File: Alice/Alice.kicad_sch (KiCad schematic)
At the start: 0 parts

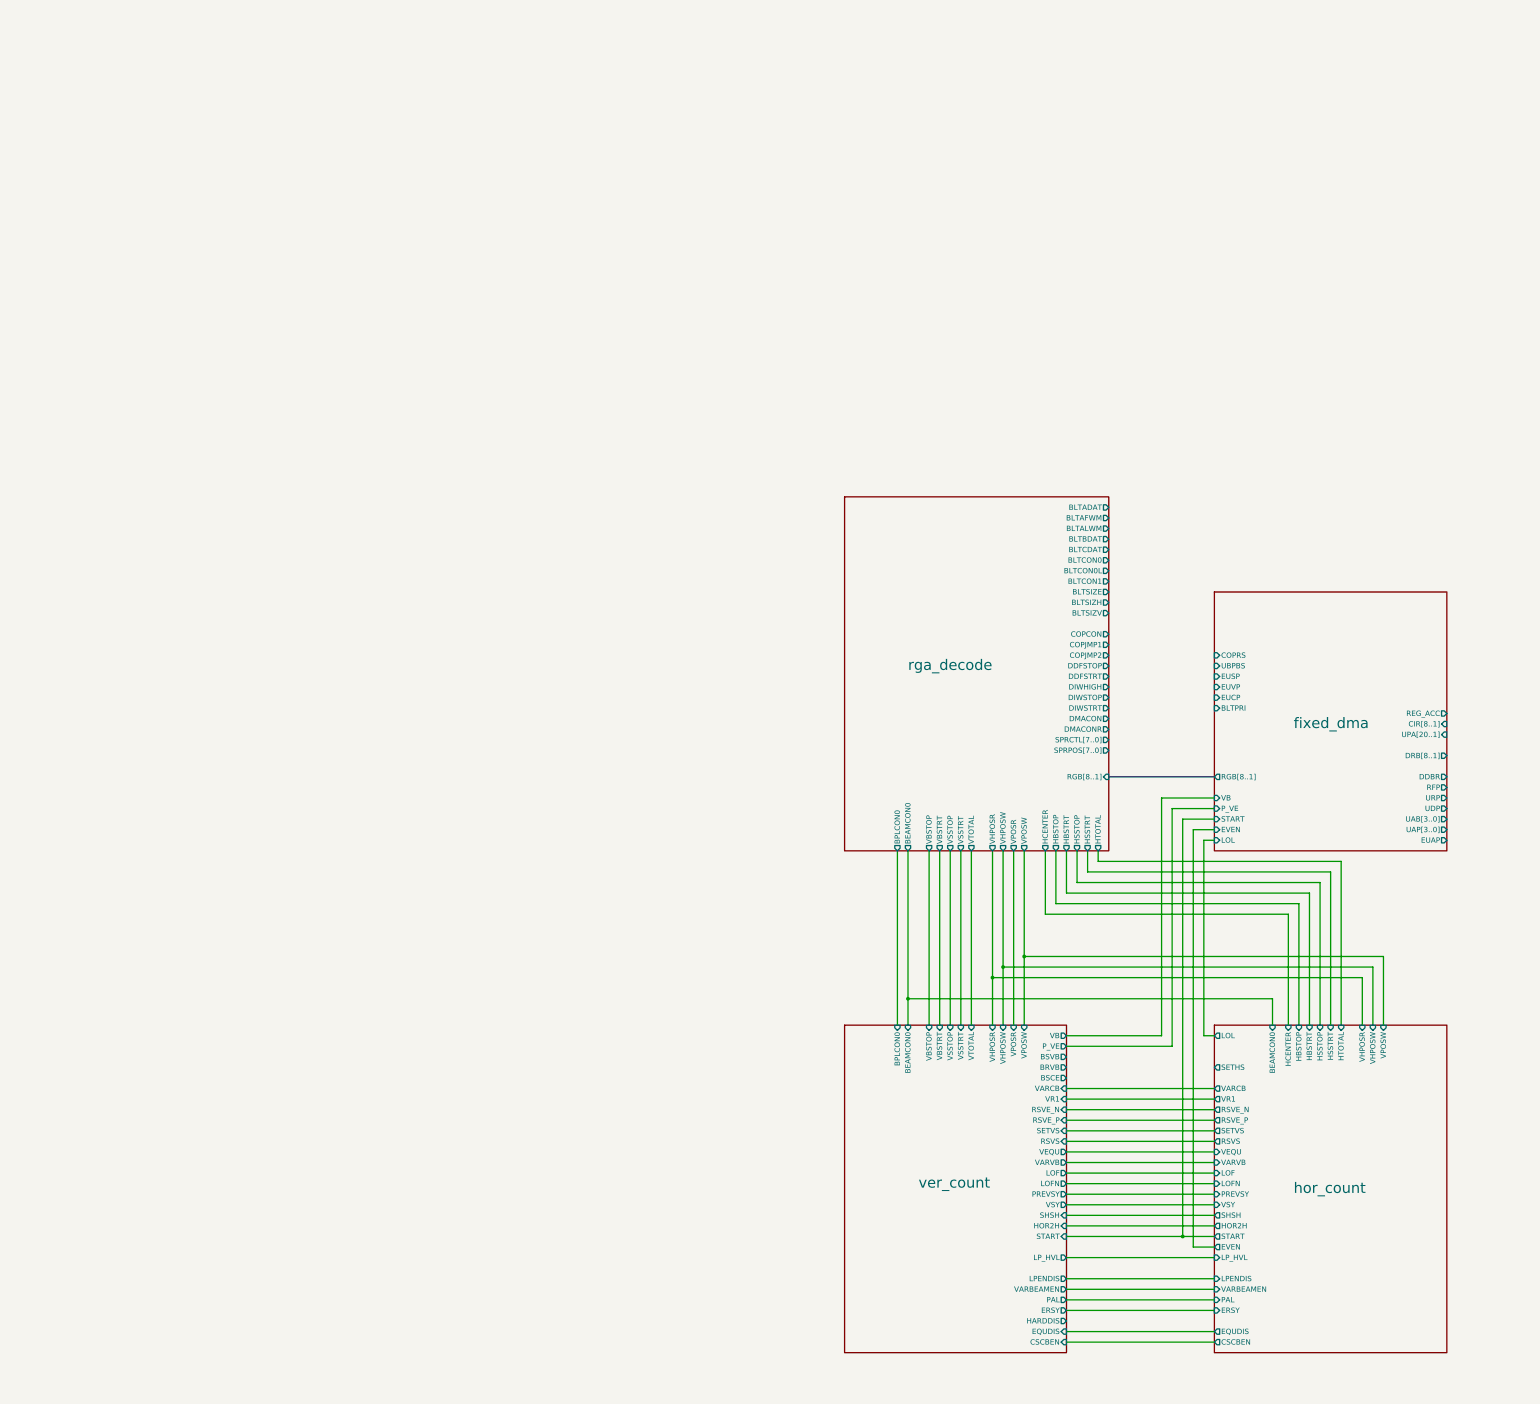
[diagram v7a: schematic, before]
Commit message: Some refactoring : BEAMCON0 and BPLCON0 moved to the top sheet, CLOCKGEN added
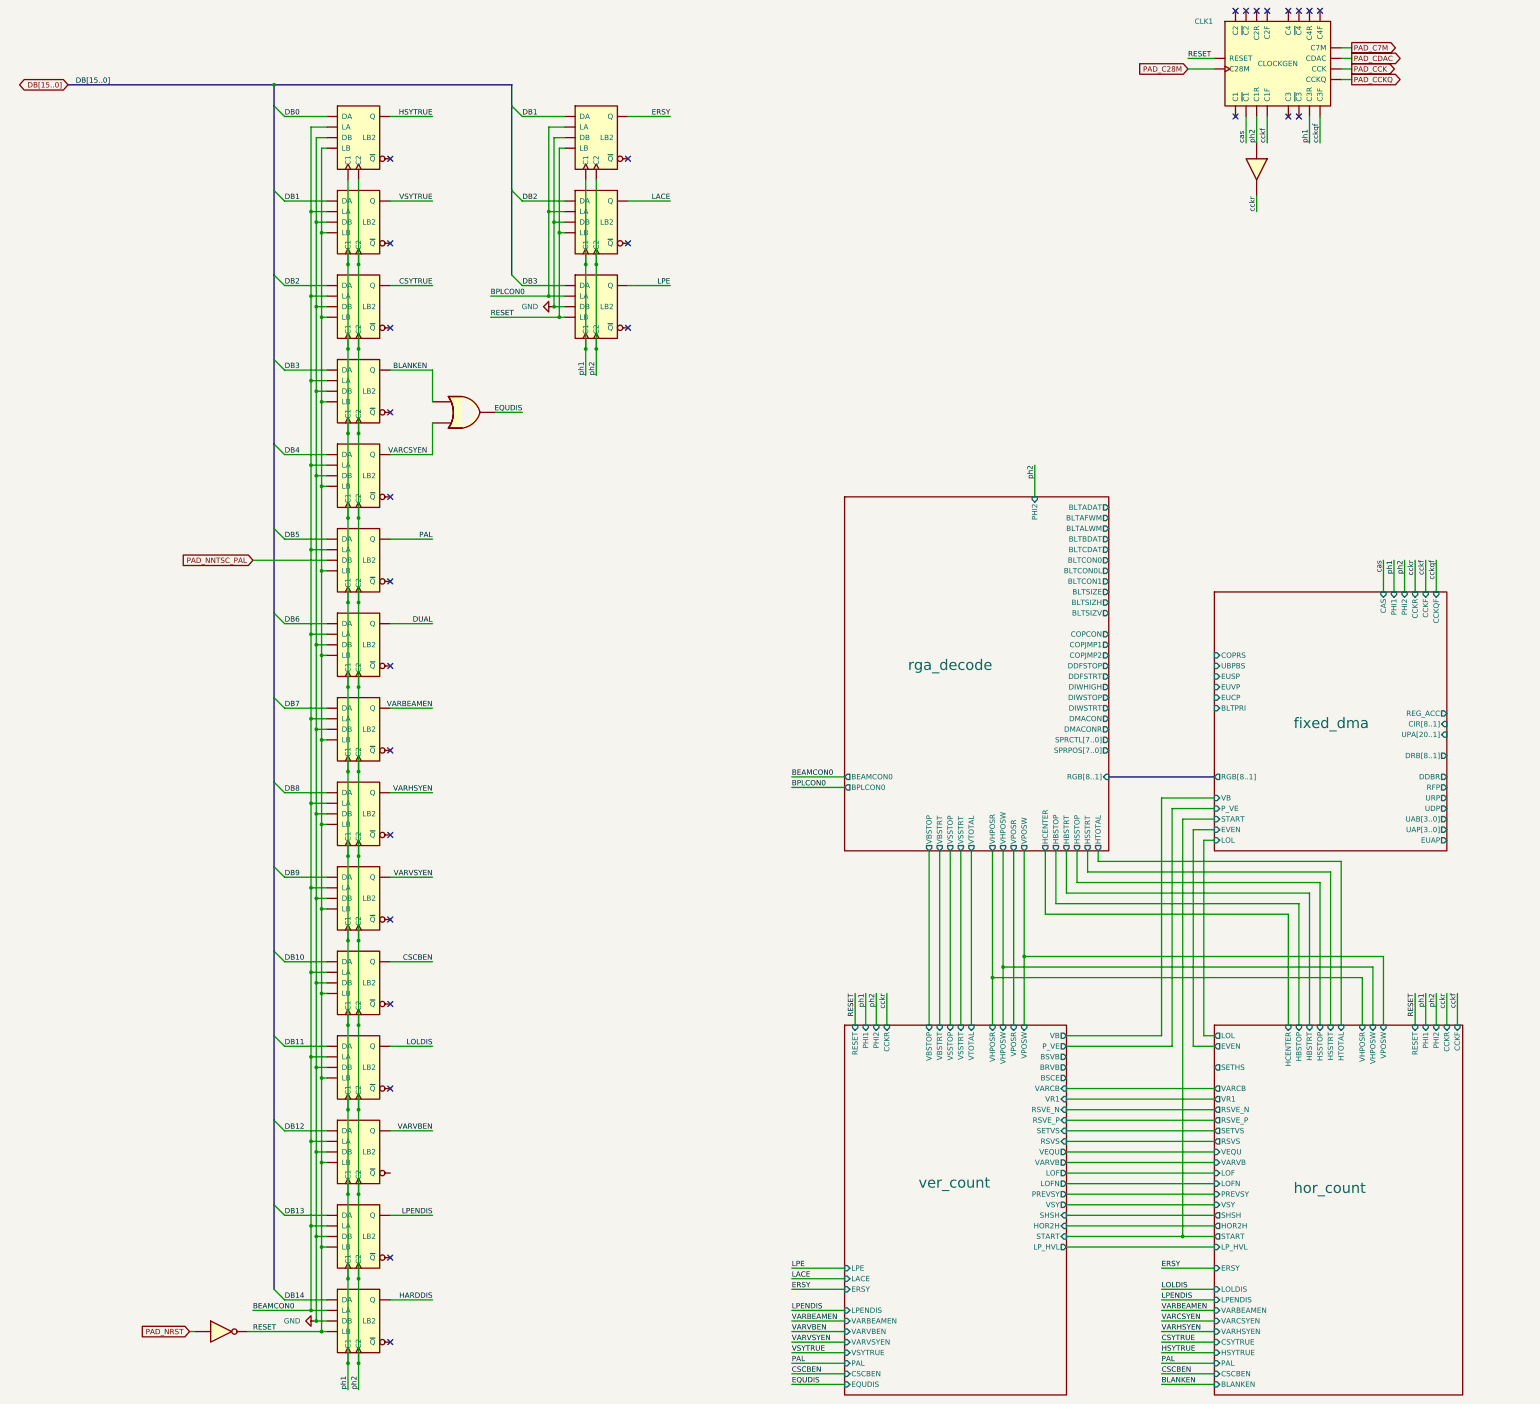
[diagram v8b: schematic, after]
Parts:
- added BEAMCON0_LB0, BEAMCON0_LB1, BEAMCON0_LB10, BEAMCON0_LB11, BEAMCON0_LB12, BEAMCON0_LB13, BEAMCON0_LB14, BEAMCON0_LB2, BEAMCON0_LB3, BEAMCON0_LB4, BEAMCON0_LB5, BEAMCON0_LB6, BEAMCON0_LB7, BEAMCON0_LB8, BEAMCON0_LB9, BPLCON0_LB1, BPLCON0_LB2, BPLCON0_LB3: LB2, symbol NMOS:LB2
- added BUF_2: BUF, symbol NMOS:BUF
- added CLK1: CLOCKGEN, symbol NMOS:CLOCKGEN
- added NOT_11: NOT, symbol NMOS:NOT
- added OR_28: OR2, symbol NMOS:OR2
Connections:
- new net BEAMCON0: BEAMCON0_LB0.2 (LA), BEAMCON0_LB1.2 (LA), BEAMCON0_LB10.2 (LA), BEAMCON0_LB11.2 (LA), BEAMCON0_LB12.2 (LA), BEAMCON0_LB13.2 (LA), BEAMCON0_LB14.2 (LA), BEAMCON0_LB2.2 (LA), BEAMCON0_LB3.2 (LA), BEAMCON0_LB4.2 (LA), BEAMCON0_LB5.2 (LA), BEAMCON0_LB6.2 (LA), BEAMCON0_LB7.2 (LA), BEAMCON0_LB8.2 (LA), BEAMCON0_LB9.2 (LA)
- new net BLANKEN: BEAMCON0_LB3.5 (Q), OR_28.2
- new net BPLCON0: BPLCON0_LB1.2 (LA), BPLCON0_LB2.2 (LA), BPLCON0_LB3.2 (LA)
- new net CSCBEN: BEAMCON0_LB10.5 (Q)
- new net CSYTRUE: BEAMCON0_LB2.5 (Q)
- new net DB0: BEAMCON0_LB0.1 (DA)
- new net DB1: BEAMCON0_LB1.1 (DA), BPLCON0_LB1.1 (DA)
- new net DB10: BEAMCON0_LB10.1 (DA)
- new net DB11: BEAMCON0_LB11.1 (DA)
- new net DB12: BEAMCON0_LB12.1 (DA)
- new net DB13: BEAMCON0_LB13.1 (DA)
- new net DB14: BEAMCON0_LB14.1 (DA)
- new net DB2: BEAMCON0_LB2.1 (DA), BPLCON0_LB2.1 (DA)
- new net DB3: BEAMCON0_LB3.1 (DA), BPLCON0_LB3.1 (DA)
- new net DB4: BEAMCON0_LB4.1 (DA)
- new net DB5: BEAMCON0_LB5.1 (DA)
- new net DB6: BEAMCON0_LB6.1 (DA)
- new net DB7: BEAMCON0_LB7.1 (DA)
- new net DB8: BEAMCON0_LB8.1 (DA)
- new net DB9: BEAMCON0_LB9.1 (DA)
- new net DUAL: BEAMCON0_LB6.5 (Q)
- new net EQUDIS: OR_28.1
- new net ERSY: BPLCON0_LB1.5 (Q)
- new net GND: BEAMCON0_LB0.3 (DB), BEAMCON0_LB1.3 (DB), BEAMCON0_LB10.3 (DB), BEAMCON0_LB11.3 (DB), BEAMCON0_LB12.3 (DB), BEAMCON0_LB13.3 (DB), BEAMCON0_LB14.3 (DB), BEAMCON0_LB2.3 (DB), BEAMCON0_LB3.3 (DB), BEAMCON0_LB4.3 (DB), BEAMCON0_LB6.3 (DB), BEAMCON0_LB7.3 (DB), BEAMCON0_LB8.3 (DB), BEAMCON0_LB9.3 (DB), BPLCON0_LB1.3 (DB), BPLCON0_LB2.3 (DB), BPLCON0_LB3.3 (DB)
- new net HARDDIS: BEAMCON0_LB14.5 (Q)
- new net HSYTRUE: BEAMCON0_LB0.5 (Q)
- new net LACE: BPLCON0_LB2.5 (Q)
- new net LOLDIS: BEAMCON0_LB11.5 (Q)
- new net LPE: BPLCON0_LB3.5 (Q)
- new net LPENDIS: BEAMCON0_LB13.5 (Q)
- new net PAD_C28M: CLK1.2 (C28M)
- new net PAD_C7M: CLK1.3 (C7M)
- new net PAD_CCK: CLK1.5 (CCK)
- new net PAD_CCKQ: CLK1.6 (CCKQ)
- new net PAD_CDAC: CLK1.4 (CDAC)
- new net PAD_NNTSC_PAL: BEAMCON0_LB5.3 (DB)
- new net PAD_NRST: NOT_11.2
- new net PAL: BEAMCON0_LB5.5 (Q)
- new net RESET: BEAMCON0_LB0.4 (LB), BEAMCON0_LB1.4 (LB), BEAMCON0_LB10.4 (LB), BEAMCON0_LB11.4 (LB), BEAMCON0_LB12.4 (LB), BEAMCON0_LB13.4 (LB), BEAMCON0_LB14.4 (LB), BEAMCON0_LB2.4 (LB), BEAMCON0_LB3.4 (LB), BEAMCON0_LB4.4 (LB), BEAMCON0_LB5.4 (LB), BEAMCON0_LB6.4 (LB), BEAMCON0_LB7.4 (LB), BEAMCON0_LB8.4 (LB), BEAMCON0_LB9.4 (LB), BPLCON0_LB1.4 (LB), BPLCON0_LB2.4 (LB), BPLCON0_LB3.4 (LB), CLK1.1 (RESET), NOT_11.1
- new net VARBEAMEN: BEAMCON0_LB7.5 (Q)
- new net VARCSYEN: BEAMCON0_LB4.5 (Q), OR_28.3
- new net VARHSYEN: BEAMCON0_LB8.5 (Q)
- new net VARVBEN: BEAMCON0_LB12.5 (Q)
- new net VARVSYEN: BEAMCON0_LB9.5 (Q)
- new net VSYTRUE: BEAMCON0_LB1.5 (Q)
- new net cas: CLK1.8 (~{C1})
- new net cckf: CLK1.10 (C1F)
- new net cckqf: CLK1.18 (C3F)
- new net cckr: BUF_2.1
- new net ph1: BEAMCON0_LB0.7 (C1), BEAMCON0_LB1.7 (C1), BEAMCON0_LB10.7 (C1), BEAMCON0_LB11.7 (C1), BEAMCON0_LB12.7 (C1), BEAMCON0_LB13.7 (C1), BEAMCON0_LB14.7 (C1), BEAMCON0_LB2.7 (C1), BEAMCON0_LB3.7 (C1), BEAMCON0_LB4.7 (C1), BEAMCON0_LB5.7 (C1), BEAMCON0_LB6.7 (C1), BEAMCON0_LB7.7 (C1), BEAMCON0_LB8.7 (C1), BEAMCON0_LB9.7 (C1), BPLCON0_LB1.7 (C1), BPLCON0_LB2.7 (C1), BPLCON0_LB3.7 (C1), CLK1.17 (C3R)
- new net ph2: BEAMCON0_LB0.8 (C2), BEAMCON0_LB1.8 (C2), BEAMCON0_LB10.8 (C2), BEAMCON0_LB11.8 (C2), BEAMCON0_LB12.8 (C2), BEAMCON0_LB13.8 (C2), BEAMCON0_LB14.8 (C2), BEAMCON0_LB2.8 (C2), BEAMCON0_LB3.8 (C2), BEAMCON0_LB4.8 (C2), BEAMCON0_LB5.8 (C2), BEAMCON0_LB6.8 (C2), BEAMCON0_LB7.8 (C2), BEAMCON0_LB8.8 (C2), BEAMCON0_LB9.8 (C2), BPLCON0_LB1.8 (C2), BPLCON0_LB2.8 (C2), BPLCON0_LB3.8 (C2), BUF_2.2, CLK1.9 (C1R)
- no-connect marks 0 -> 28
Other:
- sheet fixed_dma ports: added CAS, CCKF, CCKQF, CCKR, PHI1, PHI2; removed none
- sheet hor_count ports: added BLANKEN, CCKF, CCKR, CSYTRUE, HSYTRUE, LOLDIS, PHI1, PHI2, RESET, VARCSYEN, VARHSYEN; removed BEAMCON0, EQUDIS
- sheet rga_decode ports: added PHI2; removed none
- sheet ver_count ports: added CCKR, LACE, LPE, PHI1, PHI2, RESET, VARVBEN, VARVSYEN, VSYTRUE; removed BEAMCON0, BPLCON0, HARDDIS
